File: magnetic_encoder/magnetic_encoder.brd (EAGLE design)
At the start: 34 x 18 mm, 13 parts

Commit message: silk layer
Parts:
- renumbered U$2 to AS5600
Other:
- board text added: "3V3 INT GND"
- board text added: "AS5050A"
- board text added: "CS SCK"
- board text added: "DIR SCL SDA PGO"
- board text added: "GND OUT 3V3"
- board text added: "MOSI MISO"
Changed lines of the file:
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@@
 <setting verticaltext="up"/>
 </settings>
-<grid distance="50" unitdist="mil" unit="mil" style="lines" multiple="1" display="no" altdistance="0.025" altunitdist="inch" altunit="inch"/>
+<grid distance="12" unitdist="mil" unit="mil" style="lines" multiple="1" display="no" altdistance="0.025" altunitdist="inch" altunit="inch"/>
 <layers>
-<layer number="1" name="Top" color="4" fill="1" visible="yes" active="yes"/>
+<layer number="1" name="Top" color="4" fill="1" visible="no" active="yes"/>
 <layer number="16" name="Bottom" color="1" fill="1" visible="yes" active="yes"/>
 <layer number="17" name="Pads" color="2" fill="1" visible="yes" active="yes"/>
@@
 <layer number="23" name="tOrigins" color="15" fill="1" visible="no" active="yes"/>
 <layer number="24" name="bOrigins" color="15" fill="1" visible="yes" active="yes"/>
-<layer number="25" name="tNames" color="7" fill="1" visible="no" active="yes"/>
+<layer number="25" name="tNames" color="7" fill="1" visible="yes" active="yes"/>
 <layer number="26" name="bNames" color="7" fill="1" visible="yes" active="yes"/>
 <layer number="27" name="tValues" color="7" fill="1" visible="no" active="yes"/>
@@
 <layer number="49" name="Reference" color="7" fill="1" visible="yes" active="yes"/>
 <layer number="50" name="dxf" color="7" fill="1" visible="no" active="no"/>
-<layer number="51" name="tDocu" color="7" fill="1" visible="yes" active="yes"/>
+<layer number="51" name="tDocu" color="7" fill="1" visible="no" active="yes"/>
 <layer number="52" name="bDocu" color="7" fill="1" visible="yes" active="yes"/>
 <layer number="53" name="tGND_GNDA" color="7" fill="9" visible="no" active="no"/>
@@
 <dimension x1="0" y1="0" x2="34" y2="0" x3="17" y3="-4" textsize="1.778" layer="1"/>
 <dimension x1="0" y1="18" x2="0" y2="0" x3="-6" y3="9" textsize="1.778" layer="1"/>
+<text x="7.9248" y="13.1064" size="0.8128" layer="25" font="fixed" rot="SR270">3V3 INT   GND</text>
+<text x="15.24" y="3.175" size="0.8128" layer="25" font="fixed" rot="R90">CS SCK</text>
+<text x="14.605" y="15.5702" size="0.8128" layer="25" font="fixed" rot="R180">MOSI
+MISO</text>
+<text x="22.225" y="4.1402" size="1.016" layer="25" font="fixed" rot="R180">AS5050A</text>
+<text x="15.24" y="12.8016" size="0.8128" layer="26" font="fixed" rot="SMR270">DIR SCL SDA PGO</text>
+<text x="7.9248" y="4.8768" size="0.8128" layer="26" font="fixed" rot="SMR90">GND  OUT 3V3</text>
 </plain>
 <attributes>
@@
 </autorouter>
 <elements>
-<element name="U$1" library="austriamicrosystems" package="QFN.16" value="AS5050.QFN" x="19.2024" y="7.62"/>
-<element name="R8" library="rcl" package="R0603" value="15R" x="25.146" y="8.8392" rot="R270"/>
-<element name="C1" library="rcl" package="C0603" value="4u7" x="23.1648" y="10.3632" rot="R270"/>
-<element name="C2" library="rcl" package="C0603" value="100n" x="23.1648" y="6.858" rot="R270"/>
+<element name="U$1" library="austriamicrosystems" package="QFN.16" value="AS5050.QFN" x="19.2024" y="7.62" smashed="yes"/>
+<element name="R8" library="rcl" package="R0603" value="15R" x="25.146" y="8.8392" smashed="yes" rot="R270">
+<attribute name="NAME" x="26.416" y="10.1092" size="1.016" layer="25" font="fixed" rot="R270"/>
+<attribute name="VALUE" x="23.241" y="9.4742" size="1.27" layer="27" rot="R270"/>
+</element>
+<element name="C1" library="rcl" package="C0603" value="4u7" x="23.1648" y="10.3632" smashed="yes" rot="R270">
+<attribute name="NAME" x="22.6568" y="12.3698" size="1.016" layer="25" font="fixed"/>
+<attribute name="VALUE" x="21.2598" y="10.9982" size="1.27" layer="27" rot="R270"/>
+</element>
+<element name="C2" library="rcl" package="C0603" value="100n" x="23.1648" y="6.858" smashed="yes" rot="R270">
+<attribute name="NAME" x="22.987" y="4.1148" size="1.016" layer="25" font="fixed"/>
+<attribute name="VALUE" x="21.2598" y="7.493" size="1.27" layer="27" rot="R270"/>
+</element>
 <element name="H1" library="holes" package="2,8" value="MOUNT-HOLE2.8" x="4" y="14"/>
 <element name="H2" library="holes" package="2,8" value="MOUNT-HOLE2.8" x="4" y="4"/>
 <element name="H3" library="holes" package="2,8" value="MOUNT-HOLE2.8" x="30" y="14"/>
 <element name="H4" library="holes" package="2,8" value="MOUNT-HOLE2.8" x="30" y="4"/>
-<element name="R1" library="rcl" package="R0603" value="15R" x="15.24" y="8.9916" rot="R270"/>
-<element name="JP2" library="Headerlibrary" package="2X04" value="" x="11.5824" y="8.0772" rot="MR270"/>
-<element name="U$2" library="austriamicrosystems" package="SOIC-8" value="AS5600" x="19.2024" y="8.2804" rot="MR270"/>
-<element name="C3" library="rcl" package="C0603" value="10u" x="25.0952" y="8.0772" rot="MR0"/>
-<element name="C4" library="rcl" package="C0603" value="100n" x="25.0952" y="10.2108" rot="MR0"/>
+<element name="R1" library="rcl" package="R0603" value="15R" x="15.24" y="8.9916" smashed="yes" rot="R270">
+<attribute name="NAME" x="14.5034" y="10.795" size="1.016" layer="25" font="fixed"/>
+<attribute name="VALUE" x="13.335" y="9.6266" size="1.27" layer="27" rot="R270"/>
+</element>
+<element name="JP2" library="Headerlibrary" package="2X04" value="" x="11.5824" y="8.0772" smashed="yes" rot="MR270">
+<attribute name="VALUE" x="16.0274" y="13.1572" size="1.27" layer="28" rot="MR270"/>
+</element>
+<element name="AS5600" library="austriamicrosystems" package="SOIC-8" value="AS5600" x="19.2024" y="8.2804" smashed="yes" rot="MR270">
+<attribute name="NAME" x="21.7624" y="3.1454" size="1.016" layer="26" font="fixed" ratio="18" rot="MR0"/>
+<attribute name="VALUE" x="19.5399" y="9.8129" size="0.8128" layer="28" ratio="10" rot="MR270"/>
+</element>
+<element name="C3" library="rcl" package="C0603" value="10u" x="25.0952" y="8.0772" smashed="yes" rot="MR0">
+<attribute name="NAME" x="25.8318" y="6.096" size="1.016" layer="26" font="fixed" rot="MR0"/>
+<attribute name="VALUE" x="25.7302" y="6.1722" size="1.27" layer="28" rot="MR0"/>
+</element>
+<element name="C4" library="rcl" package="C0603" value="100n" x="25.0952" y="10.2108" smashed="yes" rot="MR0">
+<attribute name="NAME" x="25.8318" y="11.3538" size="1.016" layer="26" font="fixed" rot="MR0"/>
+<attribute name="VALUE" x="25.7302" y="8.3058" size="1.27" layer="28" rot="MR0"/>
+</element>
 </elements>
 <signals>
@@
 <vertex x="0" y="-0.1524"/>
 </polygon>
-<via x="22.8956" y="12.6096" extent="1-16" drill="0.3048"/>
+<via x="22.2606" y="12.6096" extent="1-16" drill="0.3048"/>
 <via x="20.7808" y="12.6096" extent="1-16" drill="0.3048"/>
-<contactref element="U$2" pad="4"/>
+<contactref element="AS5600" pad="4"/>
 <contactref element="C3" pad="1"/>
 <contactref element="C4" pad="1"/>
@@
 <wire x1="23.8624" y1="7.708" x2="23.1648" y2="7.708" width="0.6096" layer="1"/>
 <contactref element="C4" pad="2"/>
-<contactref element="U$2" pad="1"/>
-<contactref element="U$2" pad="2"/>
+<contactref element="AS5600" pad="1"/>
+<contactref element="AS5600" pad="2"/>
 <contactref element="C3" pad="2"/>
 <wire x1="24.2452" y1="10.2108" x2="24.2452" y2="11.9516" width="0.6096" layer="16"/>
@@
 <wire x1="17.3274" y1="10.1046" x2="15.5448" y2="11.8872" width="0.4064" layer="1"/>
 <wire x1="15.5448" y1="11.8872" x2="12.8524" y2="11.8872" width="0.4064" layer="1"/>
-<contactref element="U$2" pad="8"/>
+<contactref element="AS5600" pad="8"/>
 <wire x1="16.6224" y1="9.4954" x2="15.2442" y2="9.4954" width="0.4064" layer="16"/>
 <wire x1="15.2442" y1="9.4954" x2="12.8524" y2="11.8872" width="0.4064" layer="16"/>
@@
 <wire x1="16.002" y1="6.7056" x2="12.954" y2="6.7056" width="0.4064" layer="1"/>
 <wire x1="12.954" y1="6.7056" x2="12.8524" y2="6.8072" width="0.4064" layer="1"/>
-<contactref element="U$2" pad="6"/>
+<contactref element="AS5600" pad="6"/>
 <wire x1="16.6224" y1="6.9554" x2="13.0006" y2="6.9554" width="0.4064" layer="16"/>
 <wire x1="13.0006" y1="6.9554" x2="12.8524" y2="6.8072" width="0.4064" layer="16"/>
@@
 <wire x1="15.24" y1="9.8416" x2="13.3468" y2="9.8416" width="0.4064" layer="1"/>
 <wire x1="13.3468" y1="9.8416" x2="12.8524" y2="9.3472" width="0.4064" layer="1"/>
-<contactref element="U$2" pad="7"/>
+<contactref element="AS5600" pad="7"/>
 <wire x1="16.6224" y1="8.2254" x2="13.9742" y2="8.2254" width="0.4064" layer="16"/>
 <wire x1="13.9742" y1="8.2254" x2="12.8524" y2="9.3472" width="0.4064" layer="16"/>
@@
 <signal name="INT/OUT">
 <contactref element="U$1" pad="15"/>
-<contactref element="U$2" pad="3"/>
+<contactref element="AS5600" pad="3"/>
 <contactref element="JP2" pad="4"/>
 <wire x1="18.8774" y1="10.231" x2="18.2118" y2="10.8966" width="0.4064" layer="1"/>
@@
 </signal>
 <signal name="CS/PGO">
-<contactref element="U$2" pad="5"/>
+<contactref element="AS5600" pad="5"/>
 <contactref element="U$1" pad="4"/>
 <contactref element="JP2" pad="7"/>
@@
 </board>
 </drawing>
+<compatibility>
+<note version="6.3" minversion="6.2.2" severity="warning">
+Since Version 6.2.2 text objects can contain more than one line,
+which will not be processed correctly with this version.
+</note>
+</compatibility>
 </eagle>

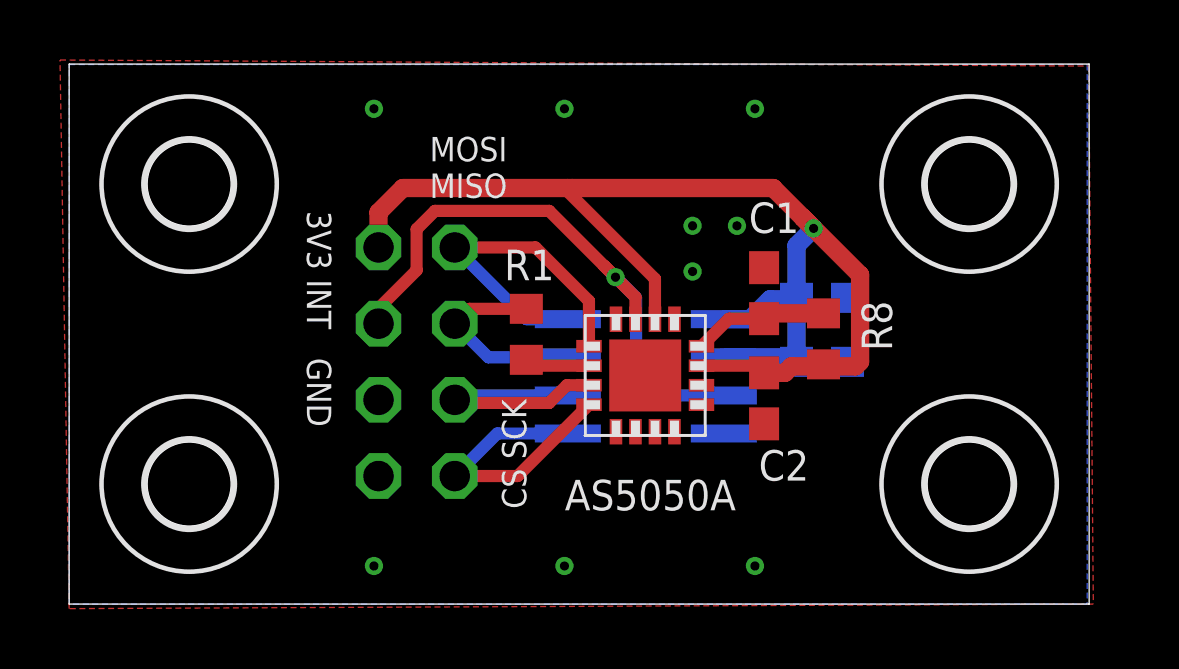
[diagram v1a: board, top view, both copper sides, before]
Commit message: measured correct dimensions
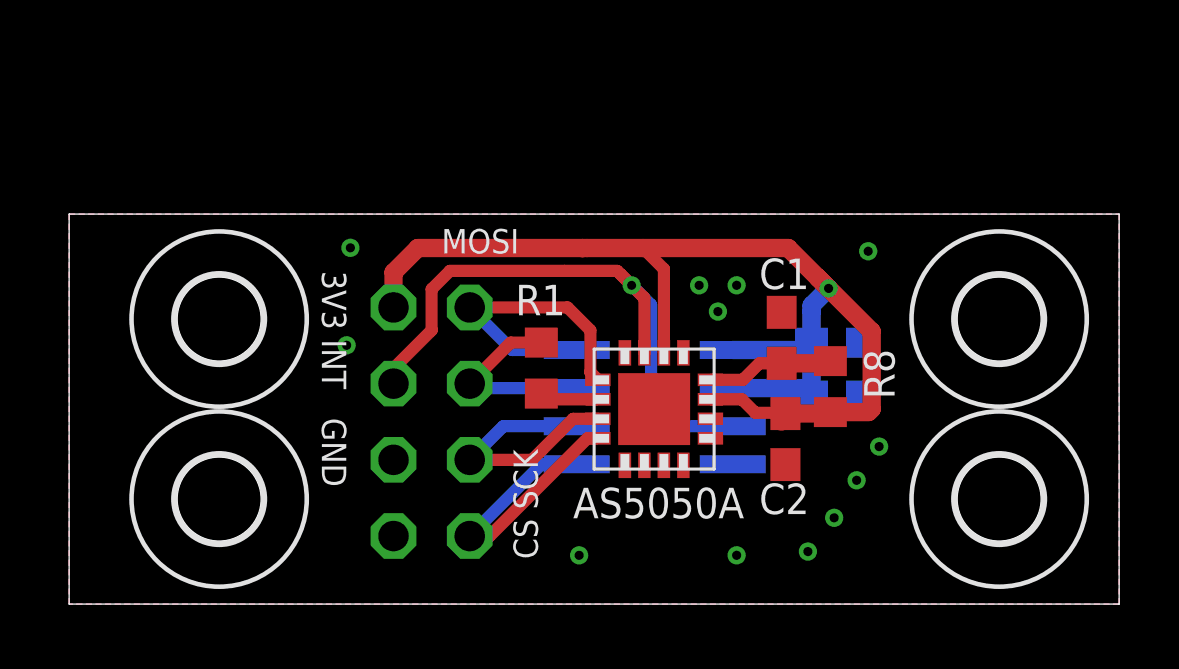
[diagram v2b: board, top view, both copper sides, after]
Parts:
- moved H1 4.61 mm to (5.00, 9.50)
- moved H3 4.61 mm to (31.0, 9.50)
- moved JP2 2.06 mm to (12.1, 6.08)
- moved R8 1.61 mm to (25.4, 7.25)
- moved C1 1.60 mm to (23.8, 8.88)
- moved C4 1.58 mm to (25.6, 8.71)
- moved C2 1.53 mm to (23.9, 5.50)
- moved R1 1.23 mm to (15.7, 7.87)
- moved C3 1.23 mm to (25.6, 6.95)
- moved U$1 1.16 mm to (19.5, 6.50)
- moved H2 1.12 mm to (5.00, 3.50)
- moved H4 1.12 mm to (31.0, 3.50)
- moved AS5600 1.07 mm to (19.5, 7.25)
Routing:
- net +3V3: track 43.2 -> 41.0 mm
- net MOSI/DIR: track 11.5 -> 10.2 mm
- net INT/OUT: track 20.1 -> 20.9 mm
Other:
- board size 34 x 18 mm -> 35 x 13 mm
- board text added: "MOSI"
- board text removed: "MOSI MISO"
